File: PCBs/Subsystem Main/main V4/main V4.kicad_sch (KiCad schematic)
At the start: 33 parts, among them J1 DCJ0303, SW1 L02P, SW2 L02P, SW3 L02P, SW4 L02P, SW5 L02P, SW6 L02P, SW7 L02P, SW8 L02P, X1 W237-103

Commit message: Fixed the headers to include reset for the SPI interface and expansion for future touch control if wanted
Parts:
- removed U$3: SPI_HEADERSPI_HEADER_RIBBON_CONNECTOR, main:SPI_HEADER_RIBBON_CONNECTOR, symbol main-eagle-import:SPI_HEADERSPI_HEADER_RIBBON_CONNECTOR
- added C1: ~, Subsystem Main Extra Symbols:SPI_HEADER_RIBBON_CONNECTOR_V2, symbol Subsystem Main Extra Symbols:SPI_HEADER_WITH_RESET
- added U2: ~, Subsystem Main Extra Symbols:T_IRQ, symbol Subsystem Main Extra Symbols:T_irq
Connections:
- net D2: now also C1.SPKR
- net D48: now also C1.SD_CS
- net D53: now also C1.TFT_CS
- net GND: now also C1.GND
- net MISO: now also C1.MISO
- net MOSI: now also C1.MOSI
- net RESET: now also C1.RST (Reset)
- net SCK: now also C1.SCK
- net at D2.1 (K): now also C1.3V3
- net at D1.1 (K): now also C1.5V
- net at U$1.D49: now also C1.TFT_DC
- net Touch_CS: now reaches U$1.A1
- net Touch_CS: now also C1.T_CS (Touch_CS)
- net at U$1.A2: now also U2.1 (T_IRQ)
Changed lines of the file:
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@@
 	(wire
 		(pts
+			(xy 346.71 200.66) (xy 350.52 200.66)
+		)
+		(stroke
+			(width 0)
+			(type default)
+		)
+	)
+	(wire
+		(pts
 			(xy 144.78 63.5) (xy 128.27 63.5)
 		)
@@
 	(wire
 		(pts
+			(xy 346.71 204.47) (xy 350.52 204.47)
+		)
+		(stroke
+			(width 0)
+			(type default)
+		)
+	)
+	(wire
+		(pts
 			(xy 123.19 99.06) (xy 123.19 92.71)
 		)
@@
 	(wire
 		(pts
+			(xy 190.5 276.86) (xy 190.5 271.78)
+		)
+		(stroke
+			(width 0)
+			(type default)
+		)
+	)
+	(wire
+		(pts
 			(xy 274.32 238.76) (xy 350.52 238.76)
 		)
@@
 	(wire
 		(pts
+			(xy 195.58 276.86) (xy 195.58 271.78)
+		)
+		(stroke
+			(width 0)
+			(type default)
+		)
+	)
+	(wire
+		(pts
 			(xy 123.19 101.6) (xy 88.9 101.6)
 		)
@@
 		)
 	)
+	(label "RESET"
+		(at 346.71 204.47 180)
+		(fields_autoplaced yes)
+		(effects
+			(font
+				(size 1.2446 1.2446)
+			)
+			(justify right bottom)
+		)
+	)
 	(label "5V"
 		(at 139.7 238.76 0)
@@
 		)
 	)
+	(label "Touch_CS"
+		(at 346.71 200.66 180)
+		(fields_autoplaced yes)
+		(effects
+			(font
+				(size 1.27 1.27)
+			)
+			(justify right bottom)
+		)
+	)
 	(label "RAW_IN"
 		(at 200.66 48.26 0)
@@
 		)
 	)
+	(label "Touch_CS"
+		(at 190.5 276.86 270)
+		(fields_autoplaced yes)
+		(effects
+			(font
+				(size 1.27 1.27)
+			)
+			(justify right bottom)
+		)
+	)
 	(label "RAW_IN"
 		(at 193.04 88.9 0)
@@
 	)
 	(symbol
+		(lib_id "Subsystem Main Extra Symbols:T_irq")
+		(at 195.58 279.4 270)
+		(unit 1)
+		(exclude_from_sim no)
+		(in_bom yes)
+		(on_board yes)
+		(dnp no)
+		(fields_autoplaced yes)
+		(property "Reference" "U2"
+			(at 198.12 281.9399 90)
+			(effects
+				(font
+					(size 1.27 1.27)
+				)
+				(justify left)
+			)
+		)
+		(property "Value" "~"
+			(at 198.12 283.845 90)
+			(effects
+				(font
+					(size 1.27 1.27)
+				)
+				(justify left)
+			)
+		)
+		(property "Footprint" "Subsystem Main Extra Symbols:T_IRQ"
+			(at 193.04 279.4 0)
+			(effects
+				(font
+					(size 1.27 1.27)
+				)
+				(hide yes)
+			)
+		)
+		(property "Datasheet" ""
+			(at 195.58 279.4 0)
+			(effects
+				(font
+					(size 1.27 1.27)
+				)
+				(hide yes)
+			)
+		)
+		(property "Description" ""
+			(at 195.58 279.4 0)
+			(effects
+				(font
+					(size 1.27 1.27)
+				)
+				(hide yes)
+			)
+		)
+		(pin "1"
+		)
+		(instances
+			(project ""
+				(path "/b46444b6-2d9e-49f7-aca9-c0067620254c"
+					(reference "U2")
+					(unit 1)
+				)
+			)
+		)
+	)
+	(symbol
 		(lib_id "main-eagle-import:L02P")
 		(at 259.08 81.28 0)
@@
 	)
 	(symbol
+		(lib_id "Subsystem Main Extra Symbols:SPI_HEADER_WITH_RESET")
+		(at 360.68 226.06 90)
+		(unit 1)
+		(exclude_from_sim no)
+		(in_bom yes)
+		(on_board yes)
+		(dnp no)
+		(fields_autoplaced yes)
+		(property "Reference" "C1"
+			(at 360.68 231.14 0)
+			(effects
+				(font
+					(size 1.27 1.27)
+				)
+				(hide yes)
+			)
+		)
+		(property "Value" "~"
+			(at 360.68 231.14 0)
+			(effects
+				(font
+					(size 1.27 1.27)
+				)
+				(hide yes)
+			)
+		)
+		(property "Footprint" "Subsystem Main Extra Symbols:SPI_HEADER_RIBBON_CONNECTOR_V2"
+			(at 367.284 226.314 0)
+			(effects
+				(font
+					(size 1.27 1.27)
+				)
+				(hide yes)
+			)
+		)
+		(property "Datasheet" ""
+			(at 360.68 231.14 0)
+			(effects
+				(font
+					(size 1.27 1.27)
+				)
+				(hide yes)
+			)
+		)
+		(property "Description" ""
+			(at 360.68 231.14 0)
+			(effects
+				(font
+					(size 1.27 1.27)
+				)
+				(hide yes)
+			)
+		)
+		(pin "MOSI"
+		)
+		(pin "MISO"
+		)
+		(pin "TFT_DC"
+		)
+		(pin "5V"
+		)
+		(pin "SPKR"
+		)
+		(pin "SCK"
+		)
+		(pin "SD_CS"
+		)
+		(pin "3V3"
+		)
+		(pin "RST"
+		)
+		(pin "GND"
+		)
+		(pin "TFT_CS"
+		)
+		(pin "T_CS"
+		)
+		(instances
+			(project ""
+				(path "/b46444b6-2d9e-49f7-aca9-c0067620254c"
+					(reference "C1")
+					(unit 1)
+				)
+			)
+		)
+	)
+	(symbol
 		(lib_id "main-eagle-import:L02P")
 		(at 279.4 182.88 180)
@@
 					(unit 1)
 				)
-			)
-		)
-	)
-	(symbol
-		(lib_id "main-eagle-import:SPI_HEADERSPI_HEADER_RIBBON_CONNECTOR")
-		(at 360.68 231.14 90)
-		(unit 1)
-		(exclude_from_sim no)
-		(in_bom yes)
-		(on_board yes)
-		(dnp no)
-		(property "Reference" "U$3"
-			(at 360.68 231.14 0)
-			(effects
-				(font
-					(size 1.27 1.27)
-				)
-				(hide yes)
-			)
-		)
-		(property "Value" "SPI_HEADERSPI_HEADER_RIBBON_CONNECTOR"
-			(at 360.68 231.14 0)
-			(effects
-				(font
-					(size 1.27 1.27)
-				)
-				(hide yes)
-			)
-		)
-		(property "Footprint" "main:SPI_HEADER_RIBBON_CONNECTOR"
-			(at 360.68 231.14 0)
-			(effects
-				(font
-					(size 1.27 1.27)
-				)
-				(hide yes)
-			)
-		)
-		(property "Datasheet" ""
-			(at 360.68 231.14 0)
-			(effects
-				(font
-					(size 1.27 1.27)
-				)
-				(hide yes)
-			)
-		)
-		(property "Description" ""
-			(at 360.68 231.14 0)
-			(effects
-				(font
-					(size 1.27 1.27)
-				)
-				(hide yes)
-			)
-		)
-		(pin "5V"
-		)
-		(pin "3V3"
-		)
-		(pin "SD_CS"
-		)
-		(pin "TFT_CS"
-		)
-		(pin "GND"
-		)
-		(pin "SPKR"
-		)
-		(pin "MISO"
-		)
-		(pin "SCK"
-		)
-		(pin "MOSI"
-		)
-		(pin "TFT_DC"
-		)
-		(instances
-			(project ""
-				(path "/b46444b6-2d9e-49f7-aca9-c0067620254c"
-					(reference "U$3")
-					(unit 1)
-				)

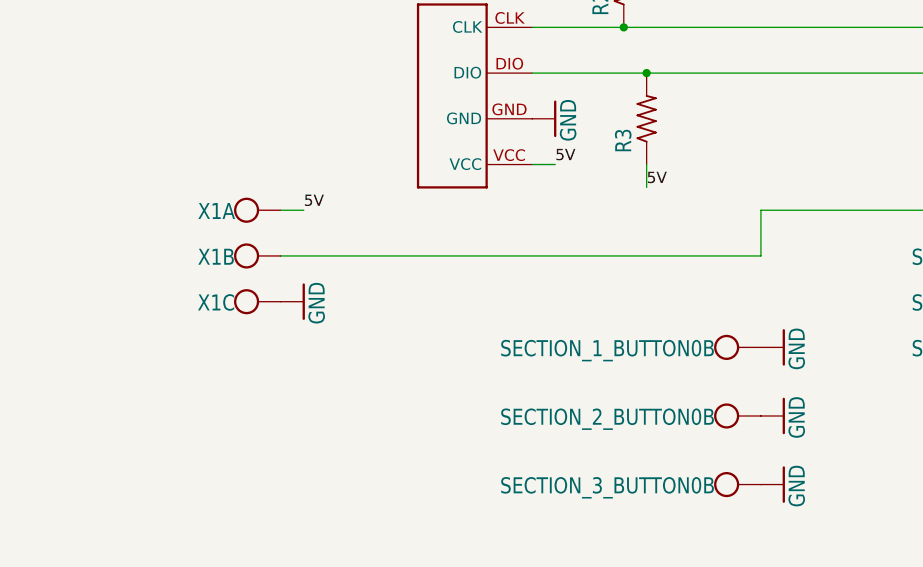
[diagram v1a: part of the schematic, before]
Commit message: added neopixel stabalization
added capacitor slot and resistor slot, both are optional but can be added to increase stability.
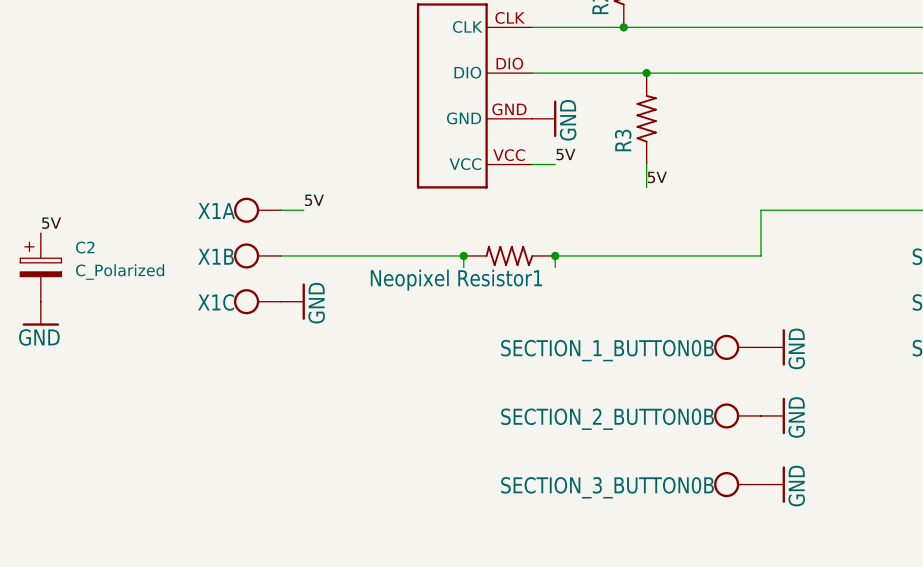
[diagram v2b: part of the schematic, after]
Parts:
- added C2: C_Polarized, Capacitor_THT:CP_Radial_D10.0mm_P2.50mm_P5.00mm, symbol Device:C_Polarized
- added Neopixel Resistor1: 350 ohm, Resistor_THT:R_Axial_DIN0204_L3.6mm_D1.6mm_P7.62mm_Horizontal, symbol main-eagle-import:FLIPFLOP-RES
- R1: value FLIPFLOP-RES -> 220 ohm
- R2: value FLIPFLOP-RES -> 10K
- R3: value FLIPFLOP-RES -> 10k
- renumbered 1 to 11
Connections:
- net 5V: now also C2.1
- net GND: now also C2.2
- net at U$1.D8: now also Neopixel Resistor1.1; no longer X1.2 (KL)
- new net: Neopixel Resistor1.2, X1.2 (KL)
